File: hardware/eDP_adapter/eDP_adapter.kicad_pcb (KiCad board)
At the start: 4 copper layers, 36.3 x 28.4 mm, 81 parts, among them J1 DF12NB(3.0)-30DS-0.5V(51), J2 DF12NB(3.0)-30DS-0.5V(51), J3 Conn_01x30, J4 Barrel_Jack_MountingPin, J5 Conn_01x06_Socket, Q1 NX3008NBKW,115, U1 NCS8801, U2 TLV62569APDRL, U3 MT3608, U5 TPNCP115ASN120T2G, X1 24MHz, CL=18PF

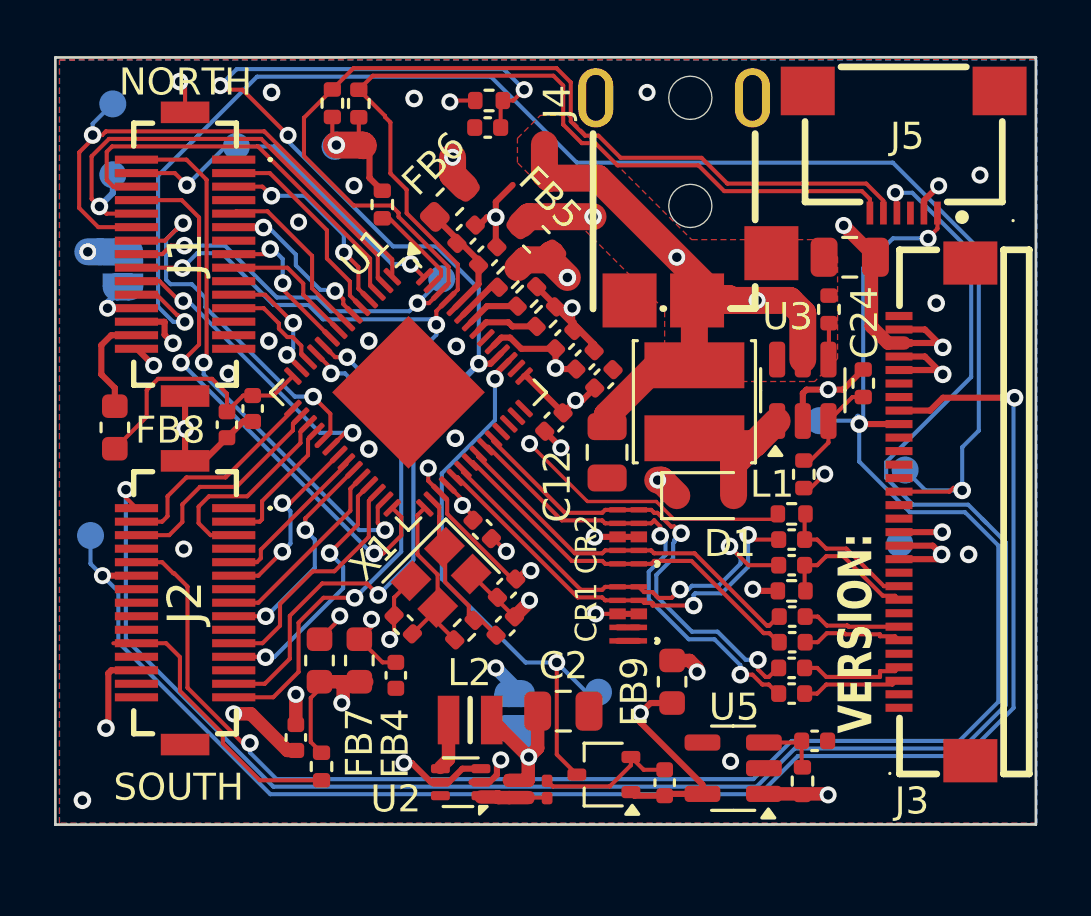
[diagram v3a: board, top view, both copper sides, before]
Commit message: change eDP adapter for dual channel LVDS input mode
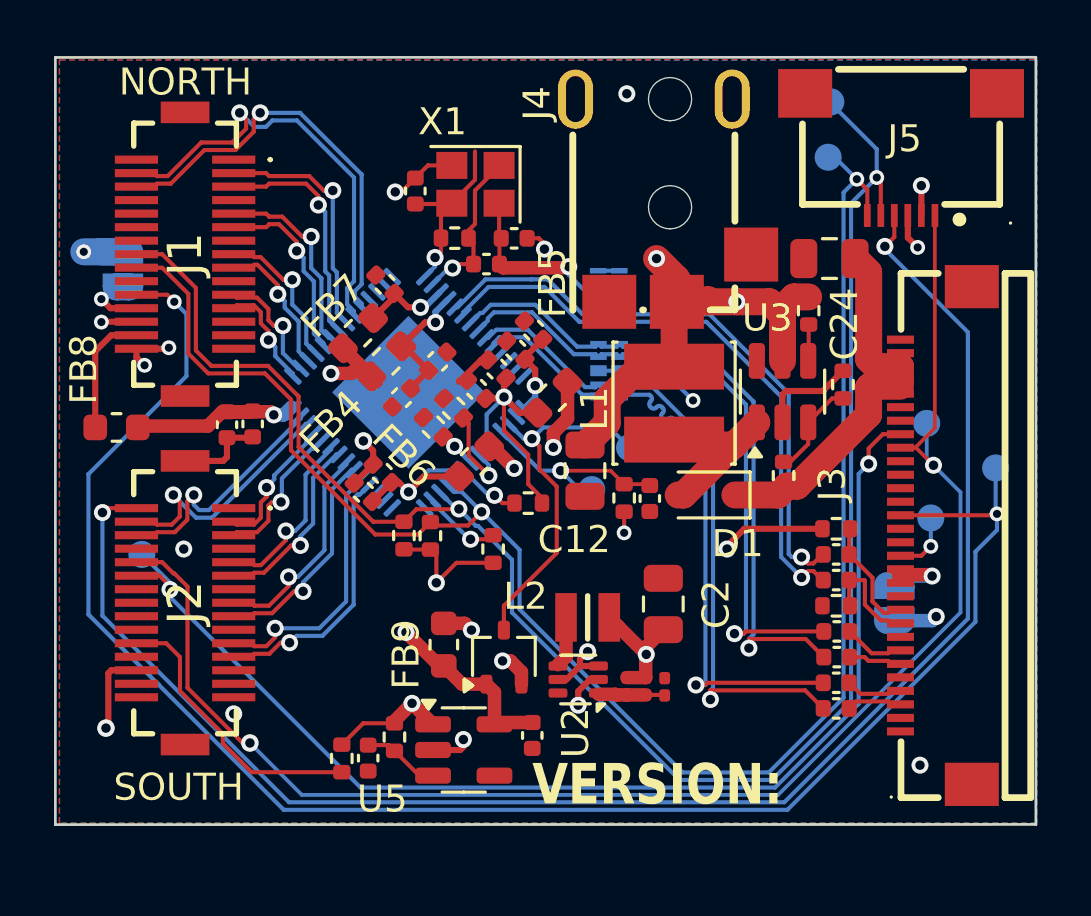
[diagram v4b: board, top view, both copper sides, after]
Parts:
- removed TP10, TP11, TP12, TP13, TP14: TestPoint_Small, TestPoint:TestPoint_Pad_D1.0mm
- added TP1: TestPoint_Small, TestPoint:TestPoint_Pad_D1.0mm, B.Cu at (132.3, 114.5)
- added TP2: TestPoint_Small, TestPoint:TestPoint_Pad_D1.0mm, B.Cu at (132.2, 116.6)
- CR1, CR2, U1: moved to B.Cu
- moved G*** 38.8 mm to (105.4, 137.8), turned to 90 degrees
- moved G*** 20.7 mm to (114.2, 116.5)
- moved C8 17.1 mm to (115.8, 121.3), turned to 135 degrees
- moved C18 16.5 mm to (115.2, 138.8), turned to -90 degrees
- moved R5 16.2 mm to (117.5, 130.6)
- moved R4 16.2 mm to (116.5, 130.6)
- moved C32 16.1 mm to (116.9, 117.8), turned to -90 degrees
- moved R14 15.5 mm to (124.7, 129.2), turned to -90 degrees
- moved R15 15.2 mm to (116.2, 138.1), turned to 90 degrees
- moved C26 15.0 mm to (125.6, 129.2), turned to -90 degrees
- moved JP2 14.6 mm to (134.7, 133.1), turned to 90 degrees
- moved X1 14.6 mm to (119.1, 117.6), turned to 180 degrees
- moved R18 14.5 mm to (118.4, 119.6), turned to 180 degrees
- moved C19 13.4 mm to (119.6, 120.6), turned to 0 degrees
- moved R6 13.4 mm to (119.8, 131.1), turned to 90 degrees
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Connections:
- J1 pad 10: LCD_HSYNC -> unconnected-(J1-9-Pad10)
- J1 pad 11: R5 -> E2-
- J1 pad 12: LCD_VSYNC -> unconnected-(J1-11-Pad12)
- J1 pad 14: G1 -> unconnected-(J1-13-Pad14)
- J1 pad 15: R2 -> E1+
- J1 pad 17: R3 -> E1-
- J1 pad 2: B1 -> unconnected-(J1-1-Pad2)
- J1 pad 20: G0 -> unconnected-(J1-19-Pad20)
- J1 pad 21: G6 -> E0+
- J1 pad 23: G7 -> E0-
- J1 pad 3: R6 -> EC+
- J1 pad 4: LCD_DE -> E3-
- J1 pad 5: R7 -> EC-
- J1 pad 6: PCLK -> E3+
- J1 pad 8: B0 -> unconnected-(J1-7-Pad8)
- J1 pad 9: R4 -> E2+
- J2 pad 11: B7 -> O2-
- J2 pad 15: B4 -> O1+
- J2 pad 17: B5 -> O1-
- J2 pad 21: B2 -> O0+
- J2 pad 23: B3 -> O0-
- J2 pad 27: R1 -> unconnected-(J2-28-Pad27)
- J2 pad 29: R0 -> unconnected-(J2-30-Pad29)
- J2 pad 3: G2 -> OC+
- J2 pad 4: G5 -> O3-
- J2 pad 5: G3 -> OC-
- J2 pad 6: G4 -> O3+
- J2 pad 9: B6 -> O2+
- U1 pad 1: LCD_VSYNC -> GND
- U1 pad 10: R1 -> OC-
- U1 pad 11: R0 -> OC+
- U1 pad 12: G7 -> O3-
- U1 pad 13: G6 -> O3+
- U1 pad 15: G5 -> E0-
- U1 pad 16: G4 -> E0+
- U1 pad 17: G3 -> E1-
- U1 pad 18: G2 -> E1+
- U1 pad 19: G1 -> E2-
- U1 pad 2: LCD_HSYNC -> GND
- U1 pad 20: G0 -> E2+
- U1 pad 21: B7 -> EC-
- U1 pad 22: B6 -> EC+
- U1 pad 23: B5 -> E3-
- U1 pad 24: B4 -> E3+
- U1 pad 25: B3 -> GND
- U1 pad 26: B2 -> GND
- U1 pad 27: B1 -> GND
- U1 pad 28: B0 -> GND
- U1 pad 3: PCLK -> GND
- U1 pad 4: R7 -> O0-
- U1 pad 5: R6 -> O0+
- U1 pad 56: LCD_DE -> GND
- U1 pad 6: R5 -> O1-
- U1 pad 7: R4 -> O1+
- U1 pad 8: R3 -> O2-
- U1 pad 9: R2 -> O2+
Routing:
- net RSTB: track 32.0 -> 7.77 mm, vias 4 -> 1
- net B0: track 20.7 -> 0.00 mm, vias 2 -> 0
- net B1: track 20.6 -> 0.00 mm, vias 2 -> 0
- net LCD_VSYNC: track 20.5 -> 0.00 mm, vias 1 -> 0
- net BACKLIGHT_POWER: track 34.3 -> 14.1 mm, vias 5 -> 0
- net R1: track 19.4 -> 0.00 mm, vias 2 -> 0
- net LCD_HSYNC: track 18.7 -> 0.00 mm, vias 1 -> 0
- net R0: track 18.5 -> 0.00 mm, vias 2 -> 0
- net XVDD_3V3: track 28.2 -> 10.5 mm, vias 4 -> 2
- net +1V2: track 33.9 -> 16.9 mm
- net SCK: track 46.6 -> 63.5 mm
- net SDA: track 49.1 -> 65.4 mm
- net E3-: track 0.00 -> 16.2 mm, vias 0 -> 1
- net E3+: track 0.00 -> 15.8 mm, vias 0 -> 1
- net PCLK: track 15.1 -> 0.00 mm
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- removed copper zone on In2.Cu, net +1V2
- removed copper zone on F.Cu, net +5V
- removed copper zone on In2.Cu, net AVDD_3V3
- removed copper zone on In1.Cu, net BACKLIGHT_POWER
- removed copper zone on In2.Cu, net DVDD_3V3
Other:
- board text added: "eDP Adapter v0.10"
- board text removed: "eDP Adapter V0.10"

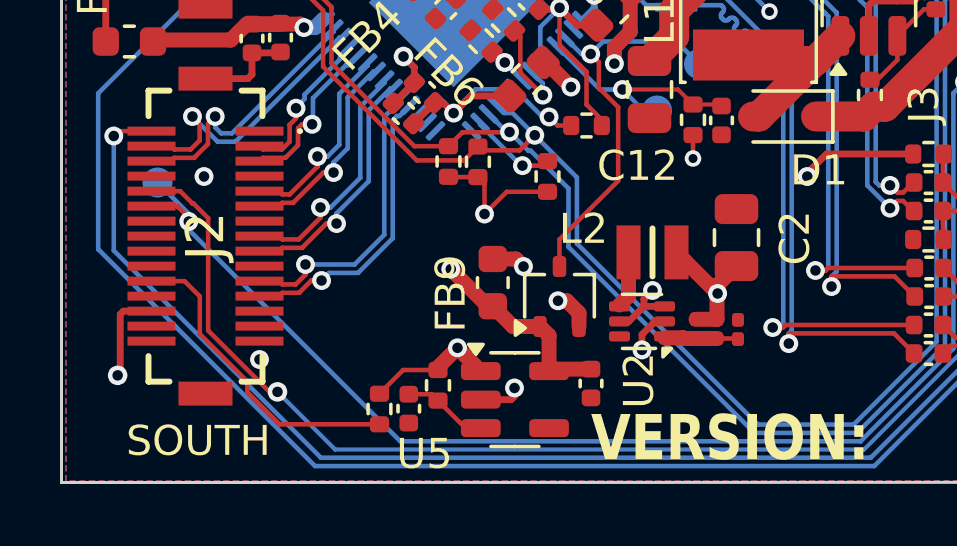
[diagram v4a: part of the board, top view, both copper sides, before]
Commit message: swap layers for better reference planes for diff pairs in eDP adapter (LVDS version)
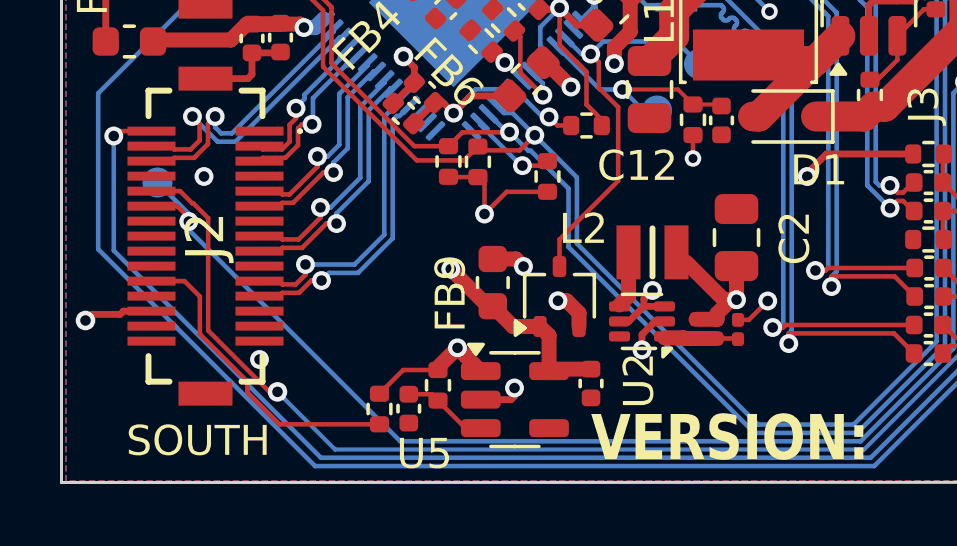
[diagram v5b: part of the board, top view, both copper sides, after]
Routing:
- net +3V3: track 76.7 -> 75.5 mm
- net GND: track 35.3 -> 35.7 mm, vias 14 -> 15
- added copper zone on In1.Cu, net +3V3
- added copper zone on In1.Cu, net +5V
- added copper zone on In2.Cu, net GND
- removed copper zone on In2.Cu, net +3V3
- removed copper zone on In2.Cu, net +5V
- removed copper zone on In1.Cu, net GND

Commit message: move 6-pin I2C FPC connector to bottom, and add missing schematics subsheets
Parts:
- J5: moved to B.Cu
- moved G*** 21.4 mm to (116.1, 137.8)
- moved TP7 13.2 mm to (132.1, 117.4)
- moved TP5 11.5 mm to (133.2, 115.3)
- moved TP6 6.93 mm to (138.1, 135.0)
- moved TP1 4.91 mm to (132.0, 119.5)
- moved TP2 4.64 mm to (133.2, 121.1)
- moved J3 3.55 mm to (136.1, 127.0)
- moved JP2 2.30 mm to (134.6, 130.8)
- moved J5 2.01 mm to (136.3, 118.0), turned to -90 degrees
- moved C15 0.51 mm to (132.1, 133.8)
- moved C17 0.51 mm to (132.1, 131.0)
- moved C23 0.51 mm to (132.1, 135.7)
- moved C1 0.51 mm to (132.1, 136.7)
- moved C14 0.51 mm to (132.1, 134.8)
- moved C16 0.51 mm to (132.1, 131.9)
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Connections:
- J3 pad 14: /IO/LCD_TEST -> /IO/TP_INT
- J3 pad 24: unconnected-(J3-Pin_24-Pad24) -> SCK
- J3 pad 25: unconnected-(J3-Pin_25-Pad25) -> SDA
- TP7 pad 1: /IO/LCD_TEST -> /IO/TP_INT
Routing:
- net GND: track 35.7 -> 43.6 mm, vias 15 -> 17
- net PSEL: track 57.0 -> 63.7 mm
- net /IO/LCD_PWM: track 44.2 -> 49.1 mm
- net TX1_N: track 2.05 -> 4.77 mm
- net +3V3_DISP: track 26.9 -> 29.5 mm
- net HPD: track 63.2 -> 65.9 mm
- net TX0_N: track 1.98 -> 4.41 mm
- net TX1_P: track 2.11 -> 4.44 mm
- net /IO/LCD_TEST: track 2.32 -> 0.00 mm, vias 1 -> 0
- net /IO/TP_INT: track 59.2 -> 61.5 mm
- net TX0_P: track 2.26 -> 3.82 mm
- net +3V3: track 75.5 -> 74.4 mm
- net SCK: track 63.5 -> 64.3 mm
- net AUX0_N: track 4.32 -> 3.69 mm

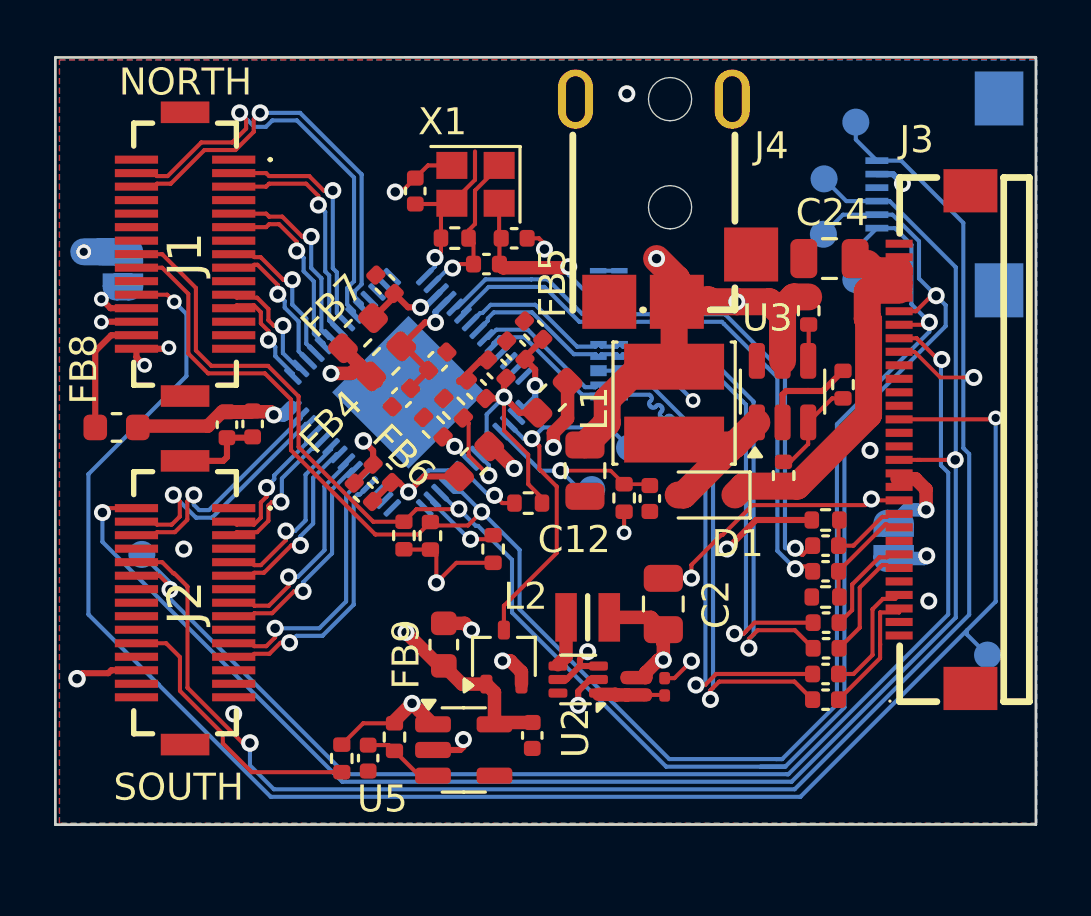
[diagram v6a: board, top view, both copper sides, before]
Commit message: change 6-pin I2C connector to one with top contacts
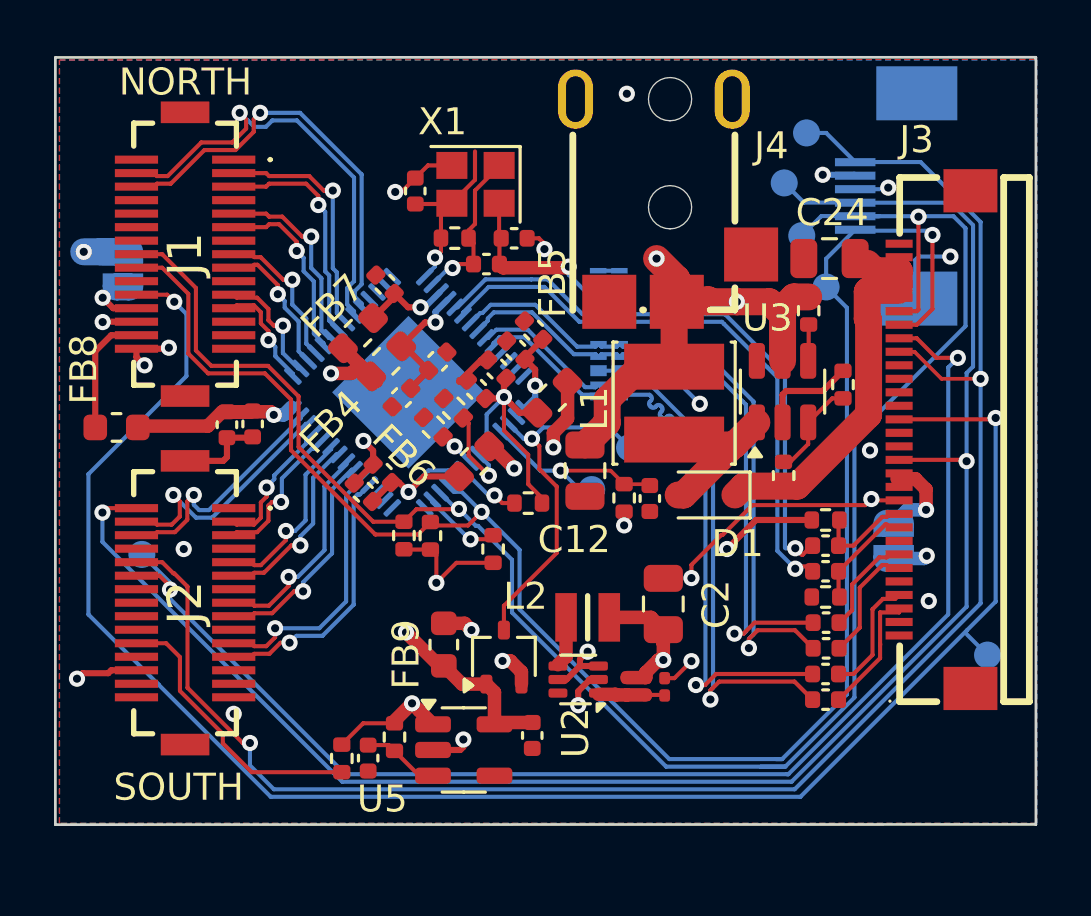
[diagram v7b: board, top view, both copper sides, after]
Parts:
- J5: footprint easyeda2kicad:FPC-SMD_FH52K-6S-0.5SH -> easyeda2kicad:CONN-SMD_527450697
- moved J5 1.92 mm to (134.3, 118.0)
- moved TP5 1.87 mm to (131.4, 115.7)
- moved TP7 1.48 mm to (130.6, 117.5)
- moved TP2 1.13 mm to (132.1, 121.4)
- moved TP1 0.80 mm to (131.2, 119.5)
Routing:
- net SDA: track 65.9 -> 72.6 mm
- net GND: track 43.6 -> 47.9 mm, vias 17 -> 19
- net /IO/TP_INT: track 61.5 -> 65.6 mm
- net +3V3: track 74.4 -> 70.9 mm
- net SCK: track 64.3 -> 67.0 mm
- net PSEL: track 63.7 -> 65.6 mm
- net /IO/LCD_PWM: track 49.1 -> 49.7 mm
